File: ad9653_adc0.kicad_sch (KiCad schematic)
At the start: 20 parts, among them J201 142-0701-201, J202 142-0701-201, J203 142-0701-201, J204 142-0701-201, U201 AD9653BCPZ-125

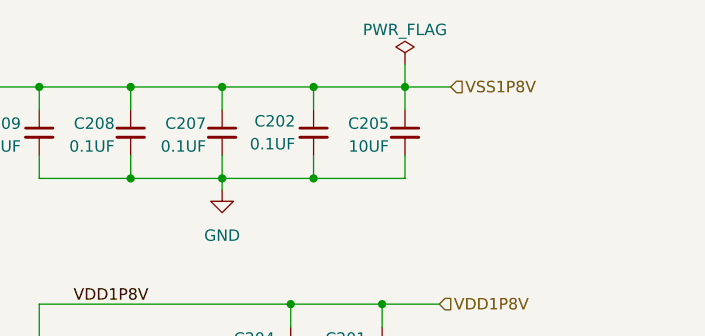
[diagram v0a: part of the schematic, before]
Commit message: resolve duplicate power flag
kicad 8 complains about two power flags on VSS1P8V net,
one each on ADC0 and ADC1 pages.  Consolidate to one
flag on the U35_LT6233 page.
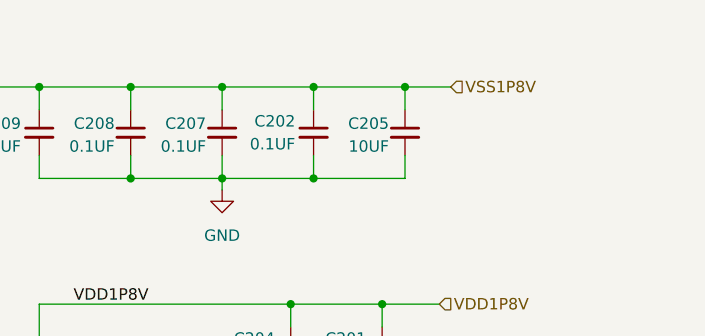
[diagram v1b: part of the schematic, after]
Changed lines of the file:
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@@
-	(wire
-		(pts
-			(xy 276.86 66.04) (xy 276.86 68.58)
-		)
-		(stroke
-			(width 0)
-			(type default)
-		)
-	)
 	(wire
 		(pts
@@
 					(unit 1)
 				)
-			)
-		)
-	)
-	(symbol
-		(lib_id "power:PWR_FLAG")
-		(at 276.86 66.04 0)
-		(mirror y)
-		(unit 1)
-		(exclude_from_sim no)
-		(in_bom yes)
-		(on_board yes)
-		(dnp no)
-		(property "Reference" "#FLG04"
-			(at 276.86 64.135 0)
-			(effects
-				(font
-					(size 1.27 1.27)
-				)
-				(hide yes)
-			)
-		)
-		(property "Value" "PWR_FLAG"
-			(at 276.86 62.23 0)
-			(effects
-				(font
-					(size 1.27 1.27)
-				)
-			)
-		)
-		(property "Footprint" ""
-			(at 276.86 66.04 0)
-			(effects
-				(font
-					(size 1.27 1.27)
-				)
-				(hide yes)
-			)
-		)
-		(property "Datasheet" "~"
-			(at 276.86 66.04 0)
-			(effects
-				(font
-					(size 1.27 1.27)
-				)
-				(hide yes)
-			)
-		)
-		(property "Description" "Special symbol for telling ERC where power comes from"
-			(at 276.86 66.04 0)
-			(effects
-				(font
-					(size 1.27 1.27)
-				)
-				(hide yes)
-			)
-		)
-		(pin "1"
-		)
-		(instances
-			(project "zest"
-				(path "/00000000-0000-0000-0000-000000000003/00000000-0000-0000-0000-000000000000"
-					(reference "#FLG04")
-					(unit 1)
-				)
